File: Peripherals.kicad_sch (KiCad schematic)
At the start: 34 parts, among them J2 Conn_01x02, J5 Conn_01x03, J6 Conn_01x03, M1 Vibrator DC Motor, U1 BMI270, U12 DRV2603RUNR, U2 OPT3004DNPR, U4 LPS22DF, U5 W25Q32JVSS, U9 MAX30102EFD_T

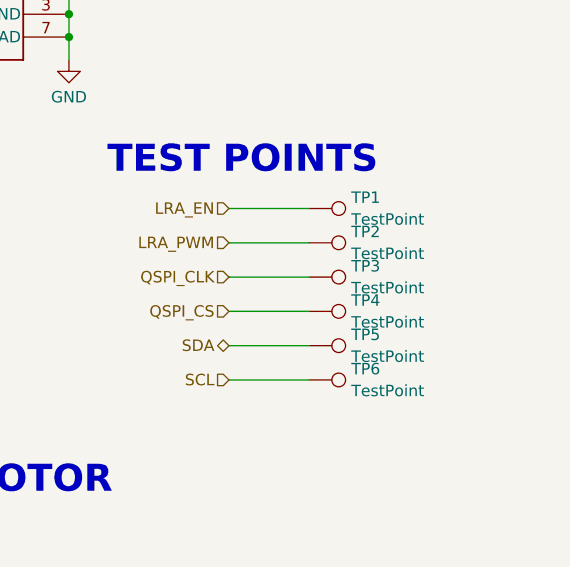
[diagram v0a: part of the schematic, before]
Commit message: New Case Files + Updated DRC Errors
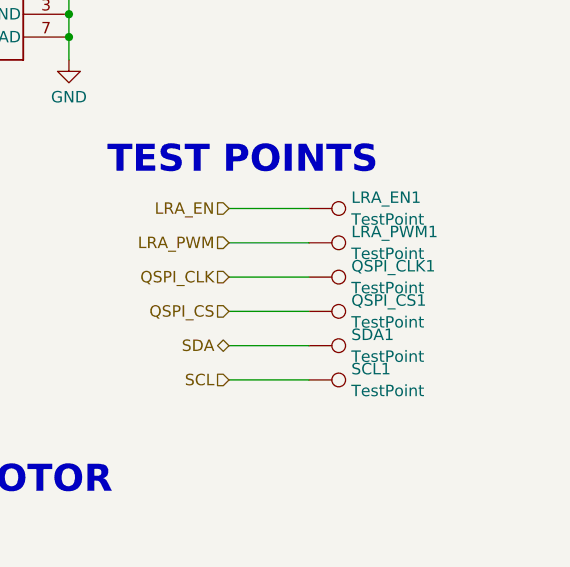
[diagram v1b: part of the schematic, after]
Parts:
- renumbered TP1 to LRA_EN1, TP2 to LRA_PWM1, TP3 to QSPI_CLK1, TP4 to QSPI_CS1, TP6 to SCL1, TP5 to SDA1
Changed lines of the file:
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@@
 		(dnp no)
 		(fields_autoplaced yes)
-		(property "Reference" "TP4"
+		(property "Reference" "QSPI_CS1"
 			(at 268.859 87.6878 90)
 			(show_name no)
@@
 			(project "Smart_Watch"
 				(path "/69095a4d-0a57-4fa3-aecb-1cfd89eedc11/bed567dd-6d09-419a-b99a-3e57c9439bd4/21b6cdb5-38b5-44be-b4b2-bd0733b126a2"
-					(reference "TP4")
+					(reference "QSPI_CS1")
 					(unit 1)
 				)
@@
 		(dnp no)
 		(fields_autoplaced yes)
-		(property "Reference" "TP3"
+		(property "Reference" "QSPI_CLK1"
 			(at 268.859 83.8778 90)
 			(show_name no)
@@
 			(project "Smart_Watch"
 				(path "/69095a4d-0a57-4fa3-aecb-1cfd89eedc11/bed567dd-6d09-419a-b99a-3e57c9439bd4/21b6cdb5-38b5-44be-b4b2-bd0733b126a2"
-					(reference "TP3")
+					(reference "QSPI_CLK1")
 					(unit 1)
 				)
@@
 		(dnp no)
 		(fields_autoplaced yes)
-		(property "Reference" "TP1"
+		(property "Reference" "LRA_EN1"
 			(at 268.859 76.2578 90)
 			(show_name no)
@@
 			(project "Smart_Watch"
 				(path "/69095a4d-0a57-4fa3-aecb-1cfd89eedc11/bed567dd-6d09-419a-b99a-3e57c9439bd4/21b6cdb5-38b5-44be-b4b2-bd0733b126a2"
-					(reference "TP1")
+					(reference "LRA_EN1")
 					(unit 1)
 				)
@@
 		(dnp no)
 		(fields_autoplaced yes)
-		(property "Reference" "TP5"
+		(property "Reference" "SDA1"
 			(at 268.859 91.4978 90)
 			(show_name no)
@@
 			(project "Smart_Watch"
 				(path "/69095a4d-0a57-4fa3-aecb-1cfd89eedc11/bed567dd-6d09-419a-b99a-3e57c9439bd4/21b6cdb5-38b5-44be-b4b2-bd0733b126a2"
-					(reference "TP5")
+					(reference "SDA1")
 					(unit 1)
 				)
@@
 		(dnp no)
 		(fields_autoplaced yes)
-		(property "Reference" "TP6"
+		(property "Reference" "SCL1"
 			(at 268.859 95.3078 90)
 			(show_name no)
@@
 			(project "Smart_Watch"
 				(path "/69095a4d-0a57-4fa3-aecb-1cfd89eedc11/bed567dd-6d09-419a-b99a-3e57c9439bd4/21b6cdb5-38b5-44be-b4b2-bd0733b126a2"
-					(reference "TP6")
+					(reference "SCL1")
 					(unit 1)
 				)
@@
 		(dnp no)
 		(fields_autoplaced yes)
-		(property "Reference" "TP2"
+		(property "Reference" "LRA_PWM1"
 			(at 268.859 80.0678 90)
 			(show_name no)
@@
 			(project "Smart_Watch"
 				(path "/69095a4d-0a57-4fa3-aecb-1cfd89eedc11/bed567dd-6d09-419a-b99a-3e57c9439bd4/21b6cdb5-38b5-44be-b4b2-bd0733b126a2"
-					(reference "TP2")
+					(reference "LRA_PWM1")
 					(unit 1)
 				)

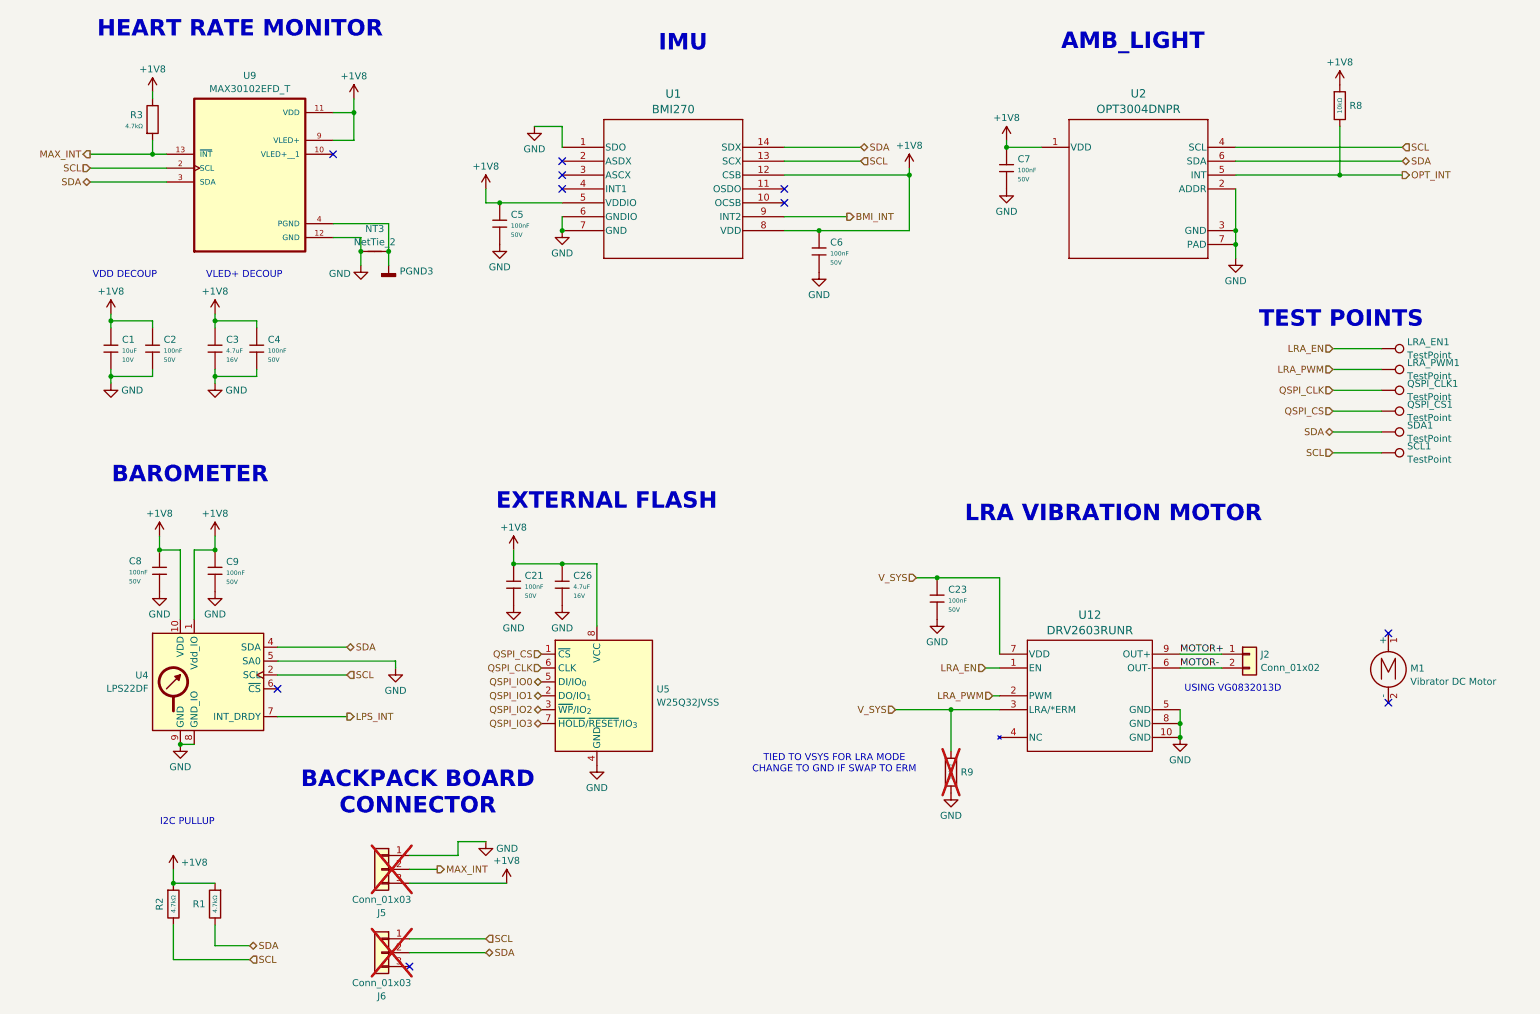
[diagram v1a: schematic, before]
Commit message: Replaced unavailable JLC components
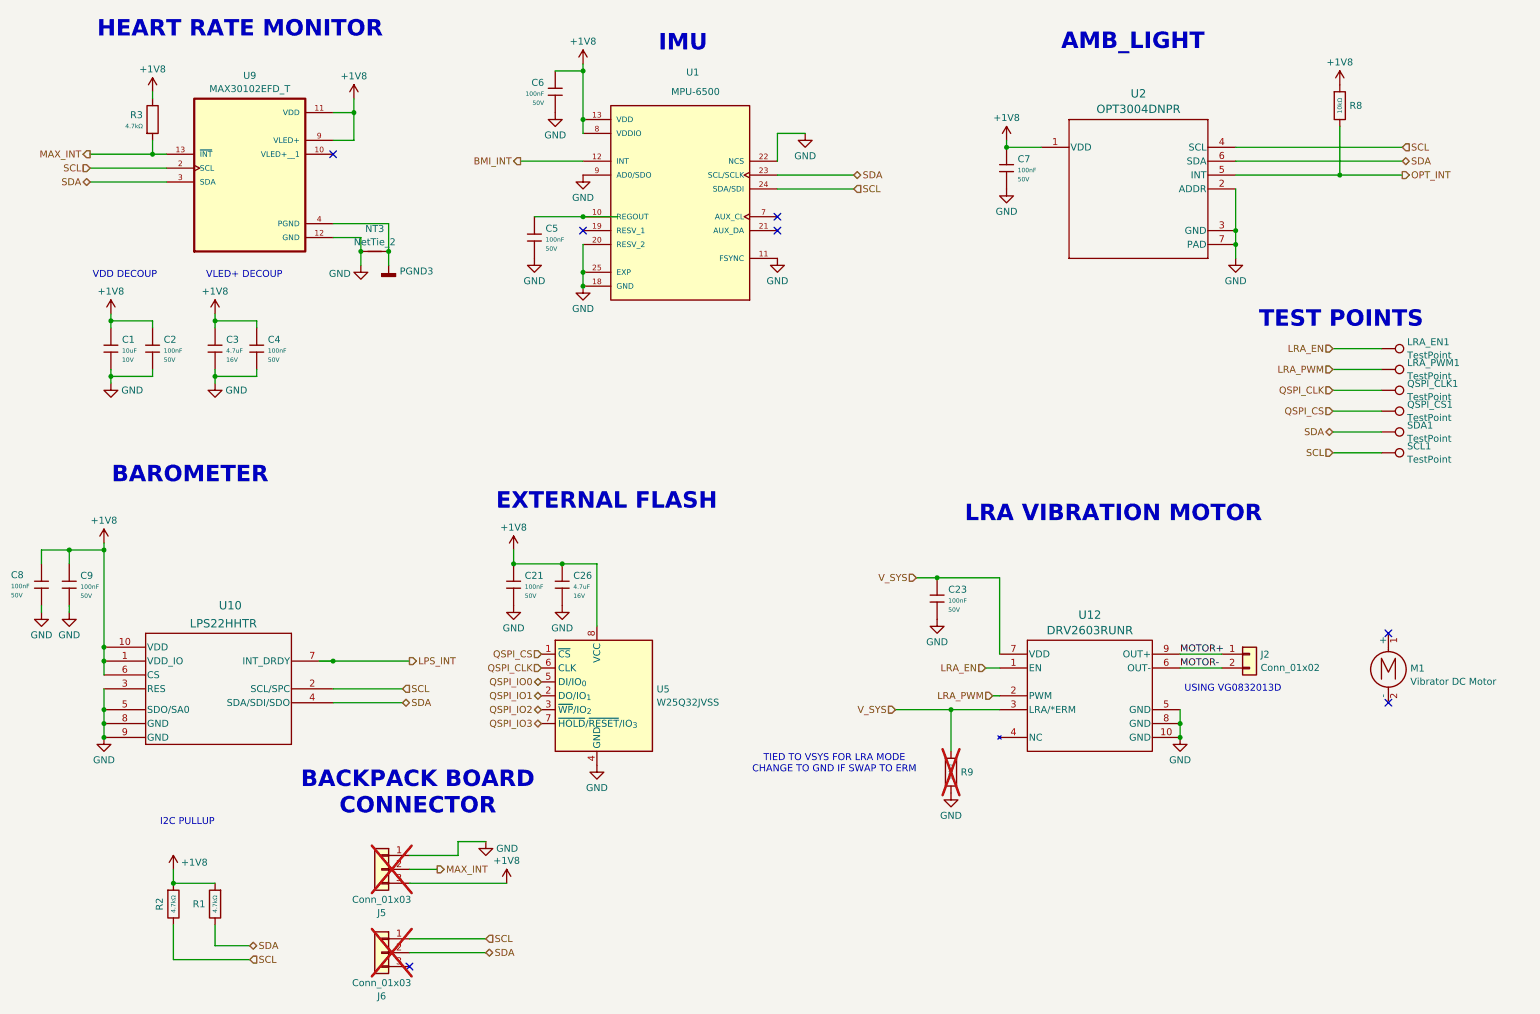
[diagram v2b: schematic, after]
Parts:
- removed U1: BMI270, Smart_Watch:BMI270_BOS-L, symbol Smart_Watch:BMI270
- removed U4: LPS22DF, Package_LGA:ST_HLGA-10_2x2mm_P0.5mm_LayoutBorder3x2y, symbol Sensor_Pressure:LPS22DF
- added U1: MPU-6500, Smart_Watch:QFN40P300X300X95-25N, symbol Smart_Watch:MPU-6500
- added U10: LPS22HHTR, Smart_Watch:HLGA-10L_2X2X0P73_STM-L, symbol Smart_Watch:LPS22HHTR
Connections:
- net +1V8: now also U1.13 (VDD), U1.8 (VDDIO), U10.1 (VDD_IO), U10.10 (VDD), U10.6 (CS); no longer C5.1
- net BMI_INT: now also U1.12 (INT)
- net GND: now also U1.11 (FSYNC), U1.18 (GND), U1.20 (RESV_2), U1.22 (NCS), U1.25 (EXP), U1.9 (AD0/SDO), U10.3 (RES), U10.5 (SDO/SA0), U10.8 (GND), U10.9 (GND)
- net LPS_INT: now also U10.7 (INT_DRDY)
- net SCL: now also U1.24 (SDA/SDI), U10.2 (SCL/SPC)
- net SDA: now also U1.23 (SCL/SCLK), U10.4 (SDA/SDI/SDO)
- new net: C5.1, U1.10 (REGOUT)
- no-connect marks 10 -> 7
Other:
- moved on the sheet: C5, C6, C8

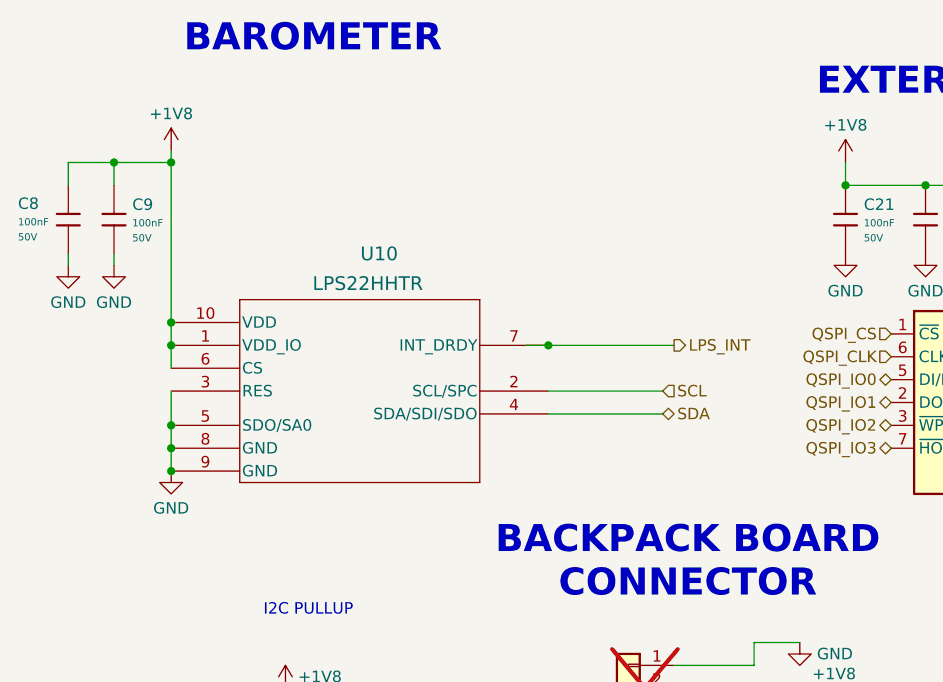
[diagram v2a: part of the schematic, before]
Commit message: Updated DRC Errors & More JLC Changes
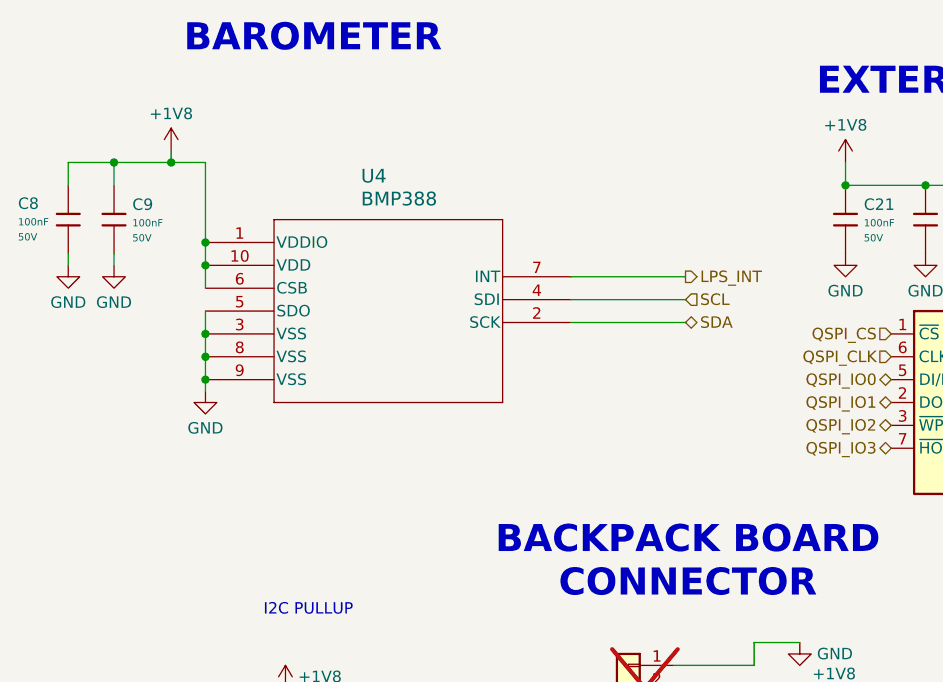
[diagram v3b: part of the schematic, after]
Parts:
- removed U10: LPS22HHTR, Smart_Watch:HLGA-10L_2X2X0P73_STM-L, symbol Smart_Watch:LPS22HHTR
- added U4: BMP388, Smart_Watch:QFN_BMP388_BOS-L, symbol Smart_Watch:BMP388
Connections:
- net +1V8: now also U4.1 (VDDIO), U4.10 (VDD), U4.6 (CSB)
- net GND: now also U4.3 (VSS), U4.5 (SDO), U4.8 (VSS), U4.9 (VSS)
- net LPS_INT: now also U4.7 (INT)
- net SCL: now also U4.4 (SDI)
- net SDA: now also U4.2 (SCK)

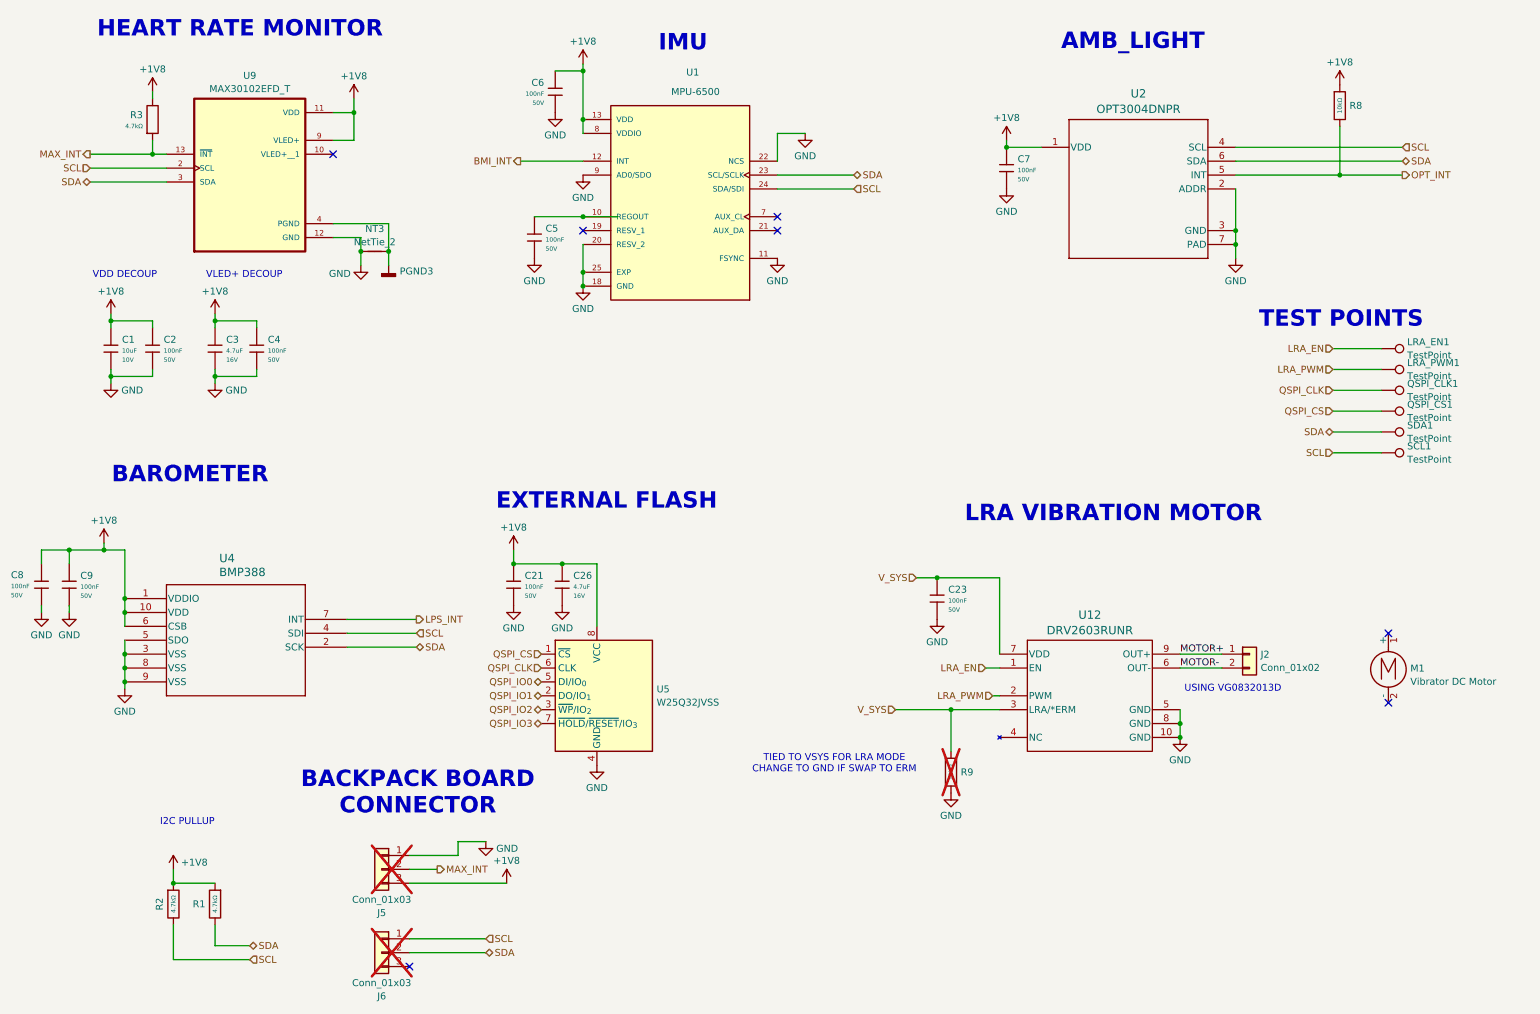
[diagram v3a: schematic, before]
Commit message: Swapped back to smaller Barometer + IMU
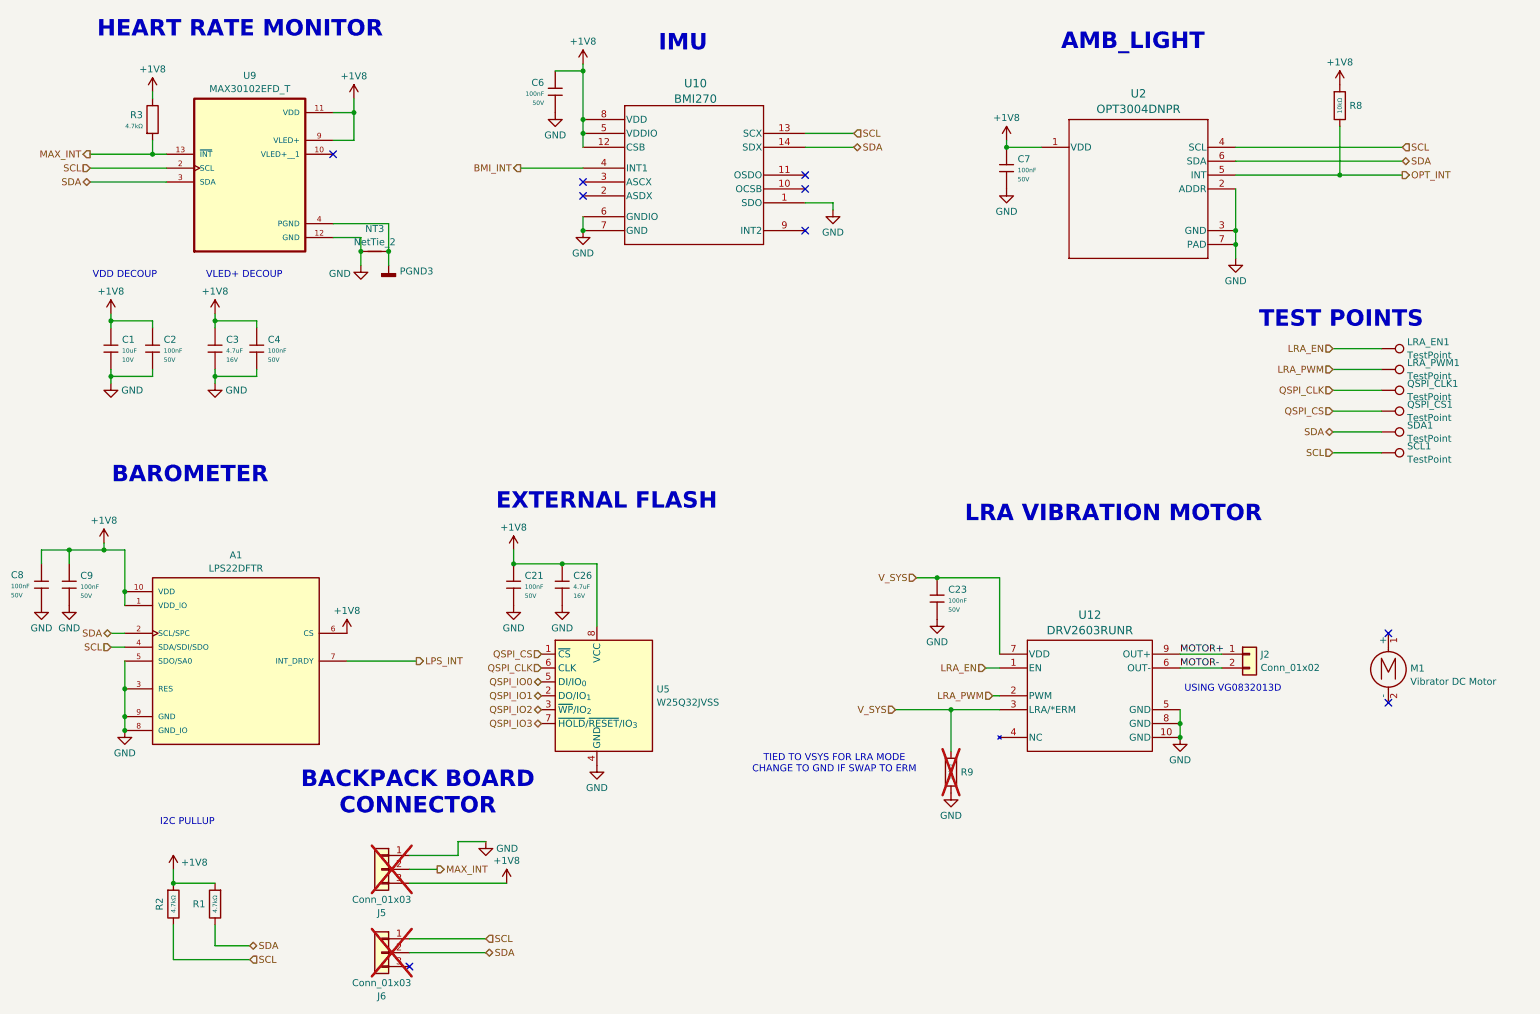
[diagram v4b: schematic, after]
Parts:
- removed C5: 100nF, PCM_JLCPCB:C_0603, symbol PCM_JLCPCB-Capacitors:0603,100nF
- removed U1: MPU-6500, Smart_Watch:QFN40P300X300X95-25N, symbol Smart_Watch:MPU-6500
- removed U4: BMP388, Smart_Watch:QFN_BMP388_BOS-L, symbol Smart_Watch:BMP388
- added A1: LPS22DFTR, Smart_Watch:XDCR_LPS22DFTR, symbol Smart_Watch:LPS22DFTR
- added U10: BMI270, Smart_Watch:BMI270_BOS-L, symbol Smart_Watch:BMI270
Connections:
- net +1V8: now also A1.1 (VDD_IO), A1.10 (VDD), A1.6 (CS), U10.12 (CSB), U10.5 (VDDIO), U10.8 (VDD)
- net BMI_INT: now also U10.4 (INT1)
- net GND: now also A1.3 (RES), A1.5 (SDO/SA0), A1.8 (GND_IO), A1.9 (GND), U10.1 (SDO), U10.6 (GNDIO), U10.7 (GND)
- net LPS_INT: now also A1.7 (INT_DRDY)
- net SCL: now also A1.4 (SDA/SDI/SDO), U10.13 (SCX)
- net SDA: now also A1.2 (SCL/SPC), U10.14 (SDX)
- no-connect marks 7 -> 9
